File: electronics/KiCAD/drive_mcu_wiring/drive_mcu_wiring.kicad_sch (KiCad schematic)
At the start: 11 parts, among them M1 goBILDA 5203 (LF), M2 goBILDA 5203 (LR), M3 goBILDA 5203 (RF), M4 goBILDA 5203 (RR), U1 NUCLEO-G474RE (drive MCU), U2 VNH5019 (LF), U3 VNH5019 (LR), U4 VNH5019 (RF), U5 VNH5019 (RR)

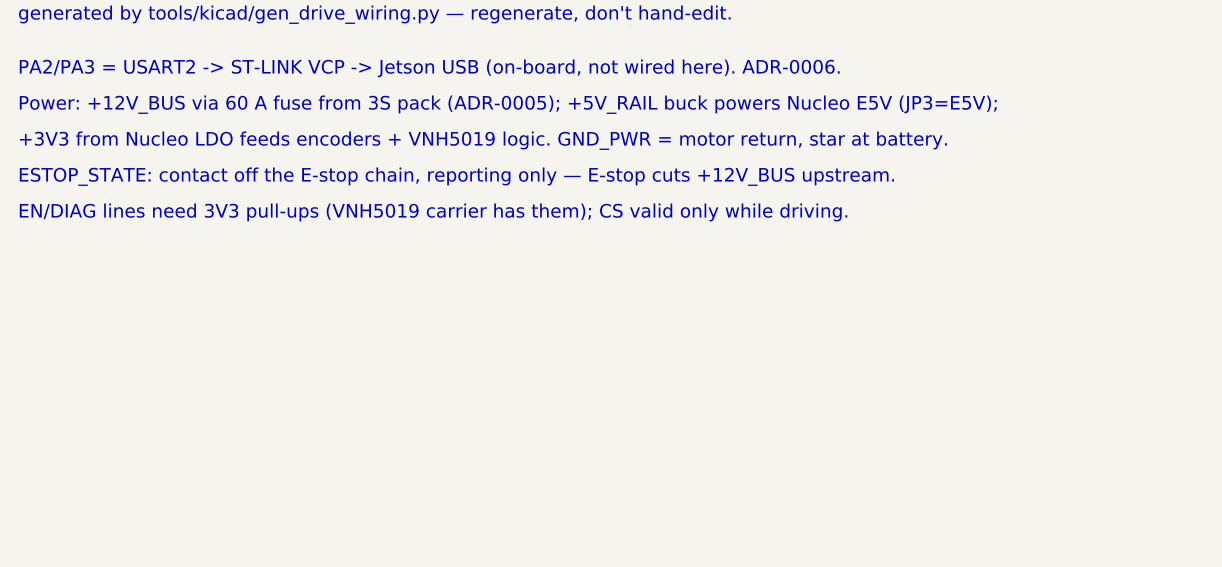
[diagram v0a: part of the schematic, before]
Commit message: System integration: six generated figures, a topology map, and a checker
Integration knowledge was spread across six correct documents and one wrong
drawing. assets/diagrams/system_architecture_mermaid.md was hand-made, not
generated, and still showed a CAN bridge two weeks after ADR-0006 chose USB
serial. Deleted. A drawing that isn't generated is already wrong; it just
hasn't been caught yet.

TOPOLOGY IS NOW DATA

docs/system_model/integration_map.yaml owns what connects to what -- ROS
nodes/topics, physical links with their connectors and cables, power rails, MCU
states, startup gates -- and may not hold a number that design_params.yaml or
the requirements yaml already owns. Where a diagram needs one it writes a
reference (param:power.protection.main_fuse_a) that buddy_calcs.integration
resolves at draw time. The fuse rating on the power diagram is not a copy of the
fuse rating; it is the fuse rating.

SIX FIGURES, regenerated by tools/build.py alongside everything else:

  ros_graph            nodes, topics, and where the system stops being ROS
  control_safety_loop  /cmd_vel to wheel, the return path, the four interlocks
  power_one_line       what is in series with what, and where each rail comes from
  interconnect         every cable, its connector, and the pin each wire lands on
  fault_state_machine  seven states, every transition, all eight fault bits
  startup_sequence     boot to motion, and the gate on each step

They render through tools/figures/blockdiagram.py, a dependency-free SVG kit --
matplotlib draws Buddy's charts well and its block diagrams badly. The palette
moved to tools/figures/palette.py, imported by all nine figures; the three
existing figures were regenerated byte-for-byte first to prove that refactor was
output-neutral.

DRIFT IS MECHANICAL, NOT HOPED FOR

tools/check_integration_map.py runs as the first step of every build and asserts
the map against pin_map.md <-> pins.h, the KiCAD net table, drive_protocol.md
(states and fault bit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
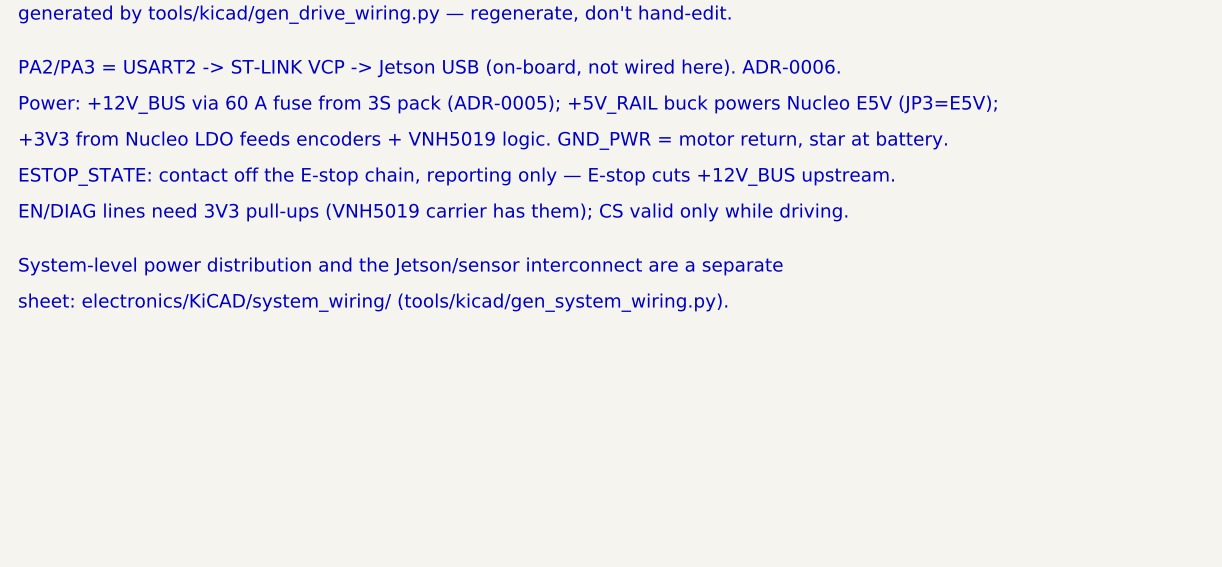
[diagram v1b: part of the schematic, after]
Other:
- note added: "System-level power distribution and the Jetson/sensor interconnect are a separate"
- note added: "sheet: electronics/KiCAD/system_wiring/ (tools/kicad/gen_system_wiring.py)."
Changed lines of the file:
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@@
 (kicad_sch
   (version 20260306)
-  (generator "gen_drive_wiring")
+  (generator "buddy_gen")
   (generator_version "10.0")
   (paper "A3")
@@
     (pin "32")
     (pin "33")
-    (instances (project "drive_mcu_wiring" (path "/c3490eb3-a813-4bee-ba1d-b9692ef23c60" (reference "U1") (unit 1))))
+    (instances (project "drive_mcu_wiring" (path "/f0e155ca-dc30-5f81-9428-2cd6185e7456" (reference "U1") (unit 1))))
   )
   (symbol (lib_id "Buddy:VNH5019_CARRIER") (at 209.55 54.61 0) (unit 1)
@@
     (pin "10")
     (pin "11")
-    (instances (project "drive_mcu_wiring" (path "/c3490eb3-a813-4bee-ba1d-b9692ef23c60" (reference "U2") (unit 1))))
+    (instances (project "drive_mcu_wiring" (path "/f0e155ca-dc30-5f81-9428-2cd6185e7456" (reference "U2") (unit 1))))
   )
   (symbol (lib_id "Buddy:GOBILDA_5203") (at 330.2 54.61 0) (unit 1)
@@
     (pin "5")
     (pin "6")
-    (instances (project "drive_mcu_wiring" (path "/c3490eb3-a813-4bee-ba1d-b9692ef23c60" (reference "M1") (unit 1))))
+    (instances (project "drive_mcu_wiring" (path "/f0e155ca-dc30-5f81-9428-2cd6185e7456" (reference "M1") (unit 1))))
   )
   (symbol (lib_id "Buddy:VNH5019_CARRIER") (at 209.55 110.49 0) (unit 1)
@@
     (pin "10")
     (pin "11")
-    (instances (project "drive_mcu_wiring" (path "/c3490eb3-a813-4bee-ba1d-b9692ef23c60" (reference "U3") (unit 1))))
+    (instances (project "drive_mcu_wiring" (path "/f0e155ca-dc30-5f81-9428-2cd6185e7456" (reference "U3") (unit 1))))
   )
   (symbol (lib_id "Buddy:GOBILDA_5203") (at 330.2 110.49 0) (unit 1)
@@
     (pin "5")
     (pin "6")
-    (instances (project "drive_mcu_wiring" (path "/c3490eb3-a813-4bee-ba1d-b9692ef23c60" (reference "M2") (unit 1))))
+    (instances (project "drive_mcu_wiring" (path "/f0e155ca-dc30-5f81-9428-2cd6185e7456" (reference "M2") (unit 1))))
   )
   (symbol (lib_id "Buddy:VNH5019_CARRIER") (at 209.55 165.1 0) (unit 1)
@@
     (pin "10")
     (pin "11")
-    (instances (project "drive_mcu_wiring" (path "/c3490eb3-a813-4bee-ba1d-b9692ef23c60" (reference "U4") (unit 1))))
+    (instances (project "drive_mcu_wiring" (path "/f0e155ca-dc30-5f81-9428-2cd6185e7456" (reference "U4") (unit 1))))
   )
   (symbol (lib_id "Buddy:GOBILDA_5203") (at 330.2 165.1 0) (unit 1)
@@
     (pin "5")
     (pin "6")
-    (instances (project "drive_mcu_wiring" (path "/c3490eb3-a813-4bee-ba1d-b9692ef23c60" (reference "M3") (unit 1))))
+    (instances (project "drive_mcu_wiring" (path "/f0e155ca-dc30-5f81-9428-2cd6185e7456" (reference "M3") (unit 1))))
   )
   (symbol (lib_id "Buddy:VNH5019_CARRIER") (at 209.55 219.71 0) (unit 1)
@@
     (pin "10")
     (pin "11")
-    (instances (project "drive_mcu_wiring" (path "/c3490eb3-a813-4bee-ba1d-b9692ef23c60" (reference "U5") (unit 1))))
+    (instances (project "drive_mcu_wiring" (path "/f0e155ca-dc30-5f81-9428-2cd6185e7456" (reference "U5") (unit 1))))
   )
   (symbol (lib_id "Buddy:GOBILDA_5203") (at 330.2 219.71 0) (unit 1)
@@
     (pin "5")
     (pin "6")
-    (instances (project "drive_mcu_wiring" (path "/c3490eb3-a813-4bee-ba1d-b9692ef23c60" (reference "M4") (unit 1))))
+    (instances (project "drive_mcu_wiring" (path "/f0e155ca-dc30-5f81-9428-2cd6185e7456" (reference "M4") (unit 1))))
   )
   (symbol (lib_id "Buddy:R_DIV") (at 59.69 214.63 0) (unit 1)
@@
     (pin "1")
     (pin "2")
-    (instances (project "drive_mcu_wiring" (path "/c3490eb3-a813-4bee-ba1d-b9692ef23c60" (reference "R1") (unit 1))))
+    (instances (project "drive_mcu_wiring" (path "/f0e155ca-dc30-5f81-9428-2cd6185e7456" (reference "R1") (unit 1))))
   )
   (symbol (lib_id "Buddy:R_DIV") (at 59.69 240.03 0) (unit 1)
@@
     (pin "1")
     (pin "2")
-    (instances (project "drive_mcu_wiring" (path "/c3490eb3-a813-4bee-ba1d-b9692ef23c60" (reference "R2") (unit 1))))
+    (instances (project "drive_mcu_wiring" (path "/f0e155ca-dc30-5f81-9428-2cd6185e7456" (reference "R2") (unit 1))))
   )
   (global_label "LF_ENC_A" (shape input) (at 59.69 152.4 180) (fields_autoplaced yes) (effects (font (size 1.27 1.27)) (justify right)))
@@
   (text "ESTOP_STATE: contact off the E-stop chain, reporting only — E-stop cuts +12V_BUS upstream." (exclude_from_sim no) (at 20 48 0) (effects (font (size 1.5 1.5)) (justify left)))
   (text "EN/DIAG lines need 3V3 pull-ups (VNH5019 carrier has them); CS valid only while driving." (exclude_from_sim no) (at 20 52 0) (effects (font (size 1.5 1.5)) (justify left)))
+  (text "System-level power distribution and the Jetson/sensor interconnect are a separate" (exclude_from_sim no) (at 20 58 0) (effects (font (size 1.5 1.5)) (justify left)))
+  (text "sheet: electronics/KiCAD/system_wiring/ (tools/kicad/gen_system_wiring.py)." (exclude_from_sim no) (at 20 62 0) (effects (font (size 1.5 1.5)) (justify left)))
   (sheet_instances (path "/" (page "1")))
   (embedded_fonts no)
